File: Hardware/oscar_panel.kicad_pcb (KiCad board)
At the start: 2 copper layers, 71 x 128.5 mm, 15 parts

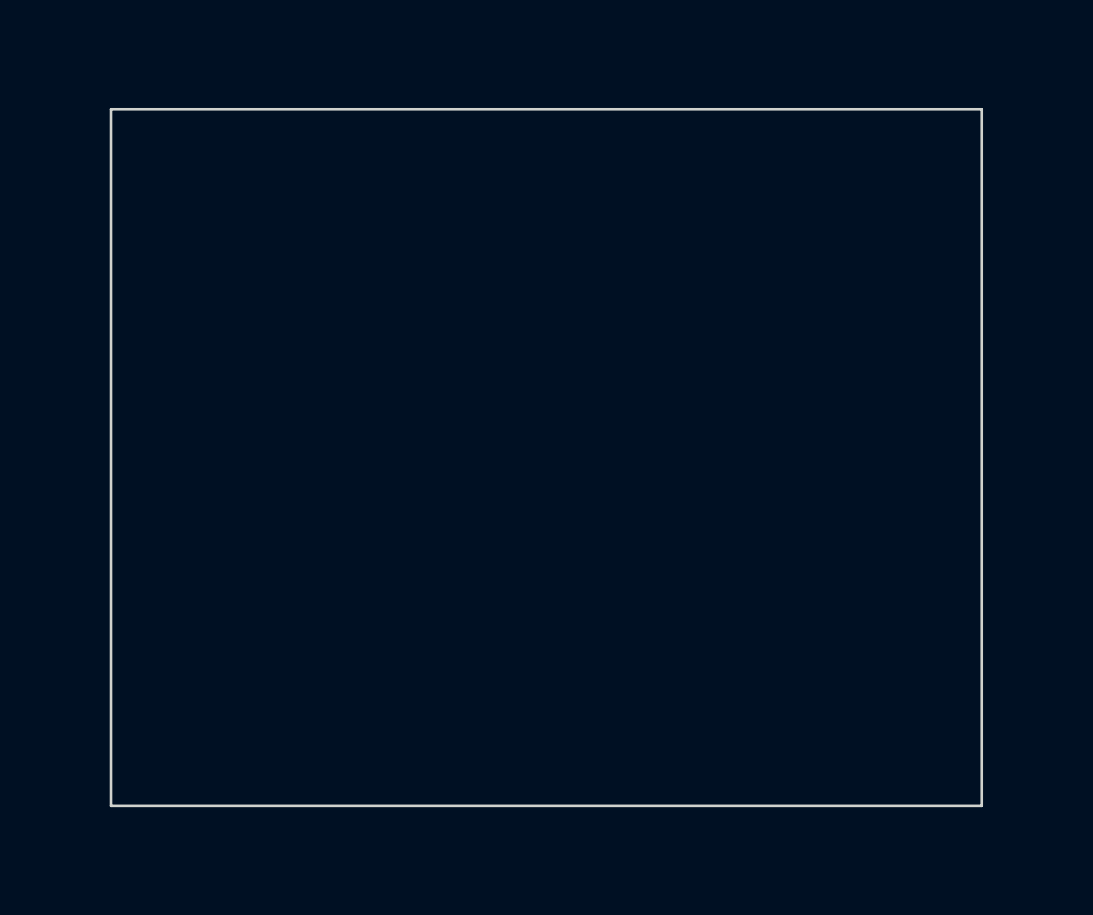
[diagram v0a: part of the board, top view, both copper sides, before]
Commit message: Added backlight logo LED
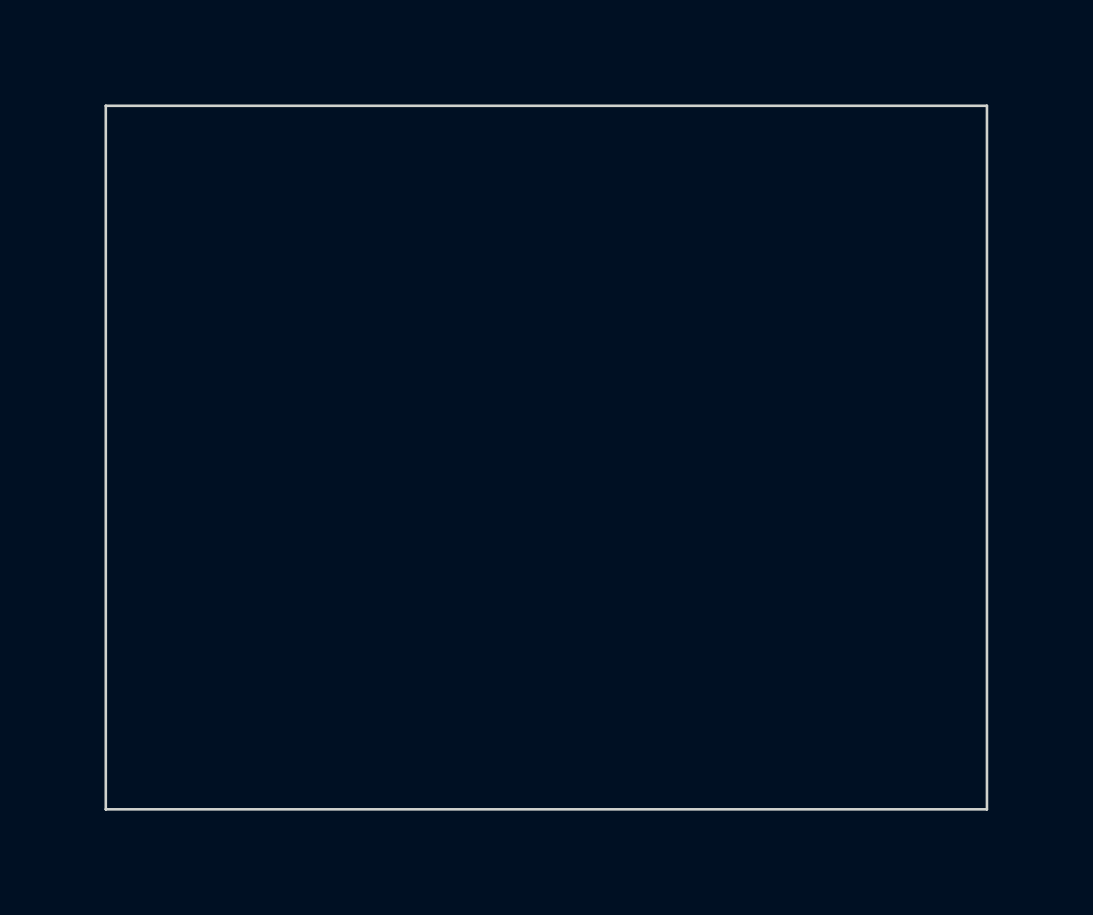
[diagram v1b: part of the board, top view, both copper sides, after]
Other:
- outline, holes or cut-outs redrawn
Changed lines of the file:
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@@
   (page A4)
   (layers
-    (0 F.Cu signal)
+    (0 F.Cu signal hide)
     (31 B.Cu signal)
     (34 B.Paste user)
@@
       (drillshape 0)
       (scaleselection 1)
-      (outputdirectory "Gerbers/"))
+      (outputdirectory "Panel_Gerbers/"))
   )
   (net 0 "")
@@
     (effects (font (size 2 2) (thickness 0.3)) (justify left))
   )
-  (gr_text JLCJLCJLCJLC (at 160 167.5) (layer B.SilkS)
+  (gr_text JLCJLCJLCJLC (at 160 167.7) (layer B.SilkS)
     (effects (font (size 1 1) (thickness 0.15)) (justify mirror))
   )
@@
   (gr_line (start 135 132.9) (end 135 154.9) (layer Eco1.User) (width 0.15))
   (gr_line (start 130.6 137) (end 188.9 137) (layer Eco1.User) (width 0.15))
-  (gr_line (start 186 93) (end 136 93) (layer Edge.Cuts) (width 0.15))
-  (gr_line (start 186 53) (end 186 93) (layer Edge.Cuts) (width 0.15))
-  (gr_line (start 136 93) (end 136 53) (layer Edge.Cuts) (width 0.15))
-  (gr_line (start 136 53) (end 186 53) (layer Edge.Cuts) (width 0.15))
+  (gr_line (start 186.3 93.2) (end 135.7 93.2) (layer Edge.Cuts) (width 0.15))
+  (gr_line (start 186.3 52.8) (end 186.3 93.2) (layer Edge.Cuts) (width 0.15))
+  (gr_line (start 135.7 93.2) (end 135.7 52.8) (layer Edge.Cuts) (width 0.15))
+  (gr_line (start 135.7 52.8) (end 186.3 52.8) (layer Edge.Cuts) (width 0.15))
   (gr_line (start 136 93) (end 136 53) (layer Eco1.User) (width 0.15))
   (gr_line (start 186 93) (end 136 93) (layer Eco1.User) (width 0.15))
@@
       )
     )
+  )
+  (zone (net 0) (net_name "") (layer B.Cu) (hatch edge 0.508)
+    (connect_pads (clearance 0.508))
+    (min_thickness 0.254)
+    (keepout (tracks not_allowed) (vias not_allowed) (copperpour not_allowed))
+    (fill (arc_segments 32) (thermal_gap 0.508) (thermal_bridge_width 0.508))
+    (polygon
+      (pts
+        (xy 125 52) (xy 196 52) (xy 196 94) (xy 125 94)
+      )
+    )
